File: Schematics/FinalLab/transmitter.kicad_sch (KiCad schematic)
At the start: 1 part

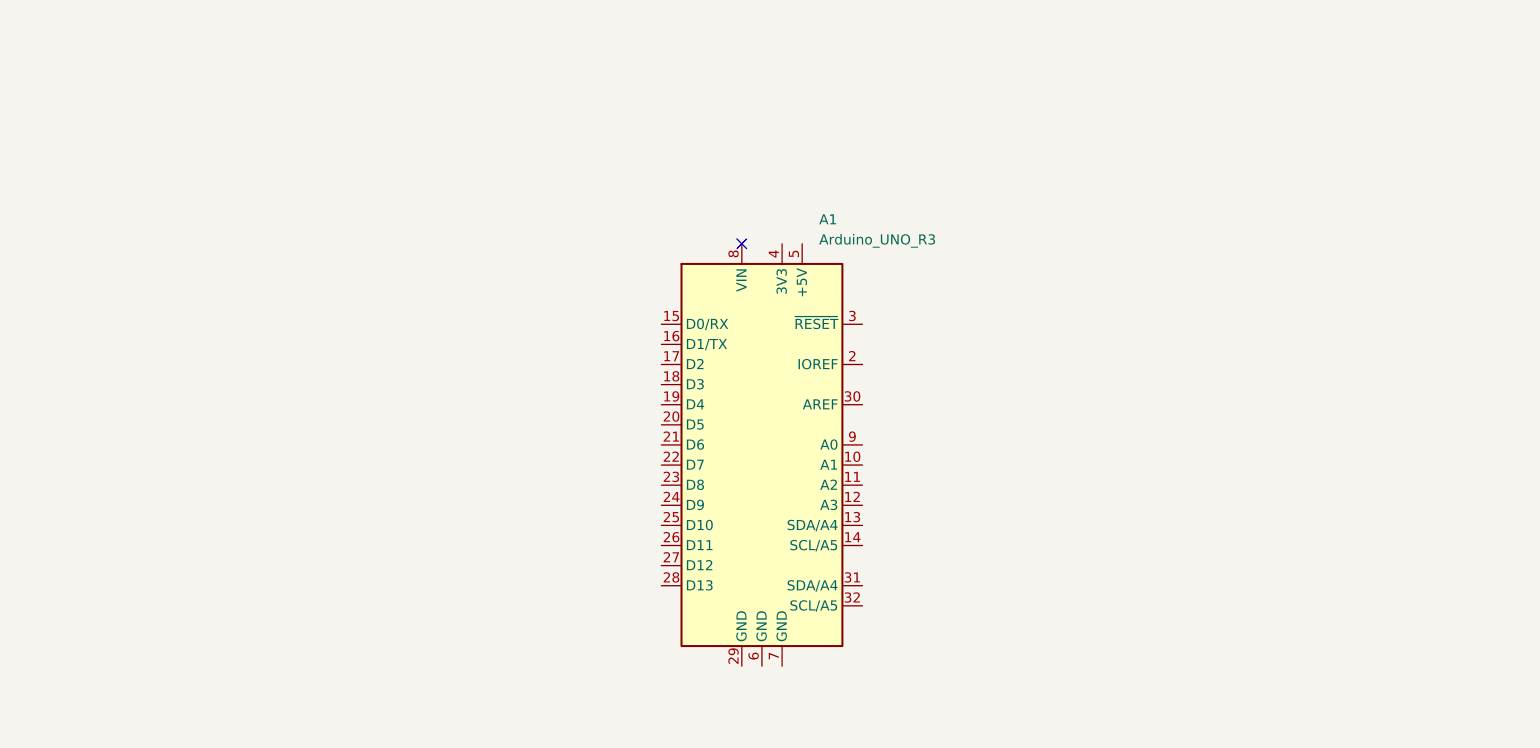
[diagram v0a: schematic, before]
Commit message: WIP
Labview is being worked on, schematic is complete, report is almost done. We need reciever code with PID stuff.
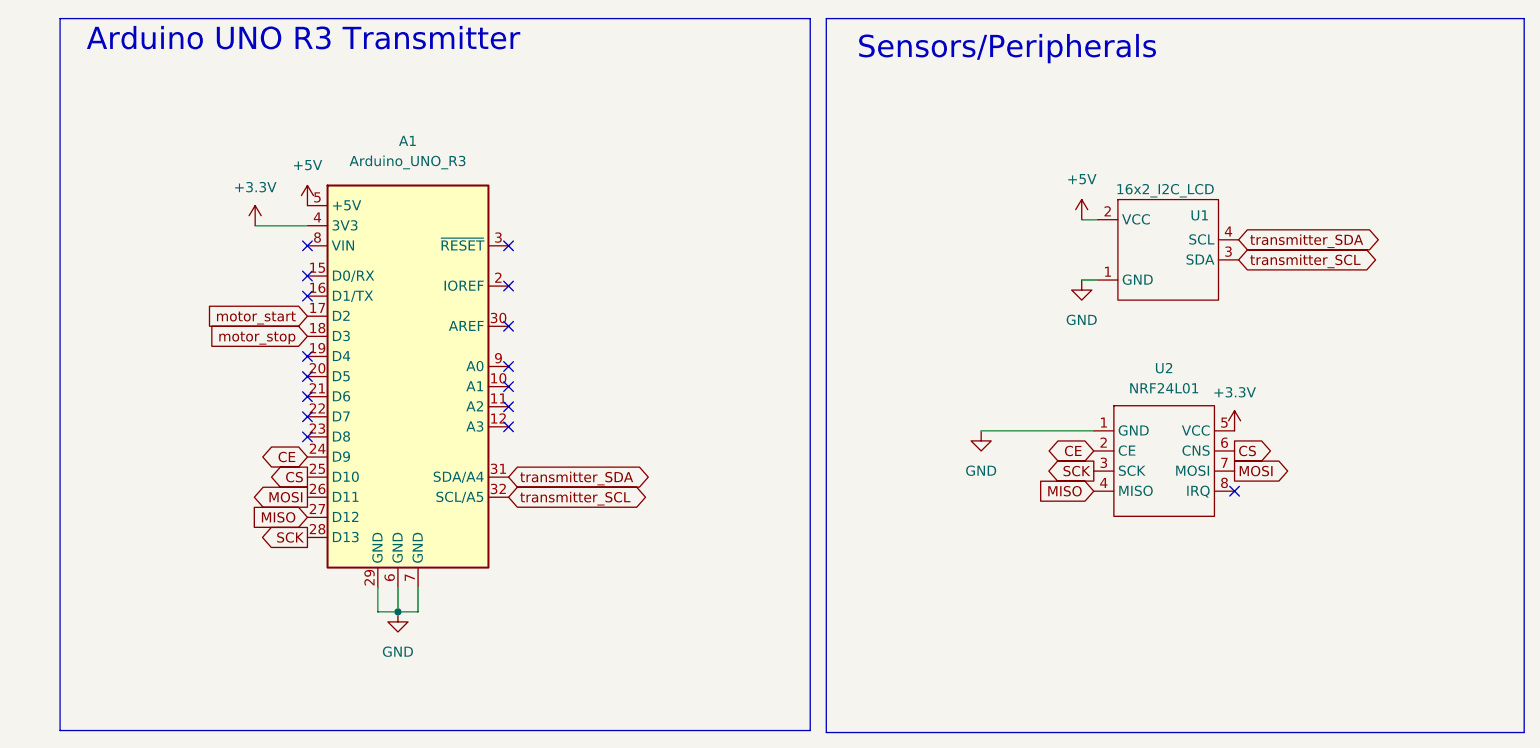
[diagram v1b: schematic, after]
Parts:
- removed A1: Arduino_UNO_R3, Module:Arduino_UNO_R3, symbol MCU_Module:Arduino_UNO_R3
- added A1: Arduino_UNO_R3, Module:Arduino_UNO_R3, symbol syms:Arduino_UNO_R3
- added U1: 16x2_I2C_LCD, symbol syms:16x2_I2C_LCD
- added U2: NRF24L01, symbol syms:NRF24L01
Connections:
- new net +3.3V: A1.4 (3V3), U2.5 (VCC)
- new net +5V: A1.5 (+5V), U1.2 (VCC)
- new net CE: A1.24 (D9), U2.2 (CE)
- new net CS: A1.25 (D10), U2.6 (CNS)
- new net GND: A1.29 (GND), A1.6 (GND), A1.7 (GND), U1.1 (GND), U2.1 (GND)
- new net MISO: A1.27 (D12), U2.4 (MISO)
- new net MOSI: A1.26 (D11), U2.7 (MOSI)
- new net SCK: A1.28 (D13), U2.3 (SCK)
- new net motor_start: A1.17 (D2)
- new net motor_stop: A1.18 (D3)
- new net transmitter_SCL: A1.32 (SCL/A5), U1.3 (SDA)
- new net transmitter_SDA: A1.31 (SDA/A4), U1.4 (SCL)
- no-connect marks 1 -> 16
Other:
- note added: "Arduino UNO R3 Transmitter"
- note added: "Sensors/Peripherals"
